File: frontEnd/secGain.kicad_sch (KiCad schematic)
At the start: 11 parts, among them U601 BGS12P2L6E6327XTSA1, U602 MSA-0286, U603 BGS12P2L6E6327XTSA1

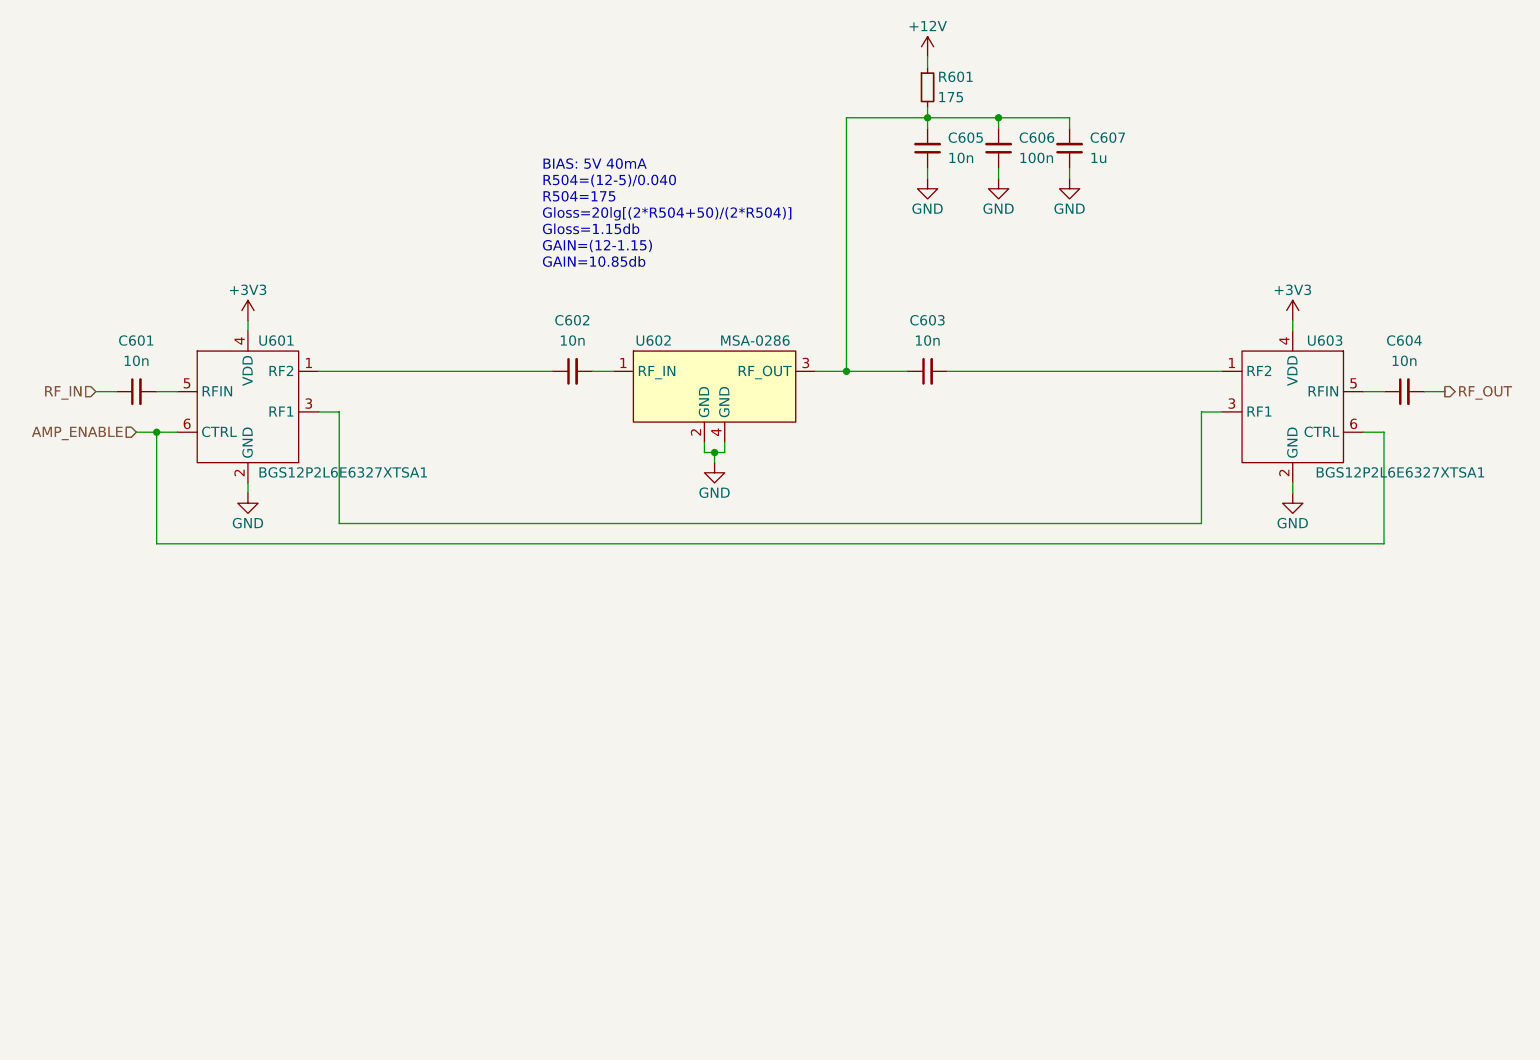
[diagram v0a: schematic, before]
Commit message: update schematics, add bypass for the attenuator
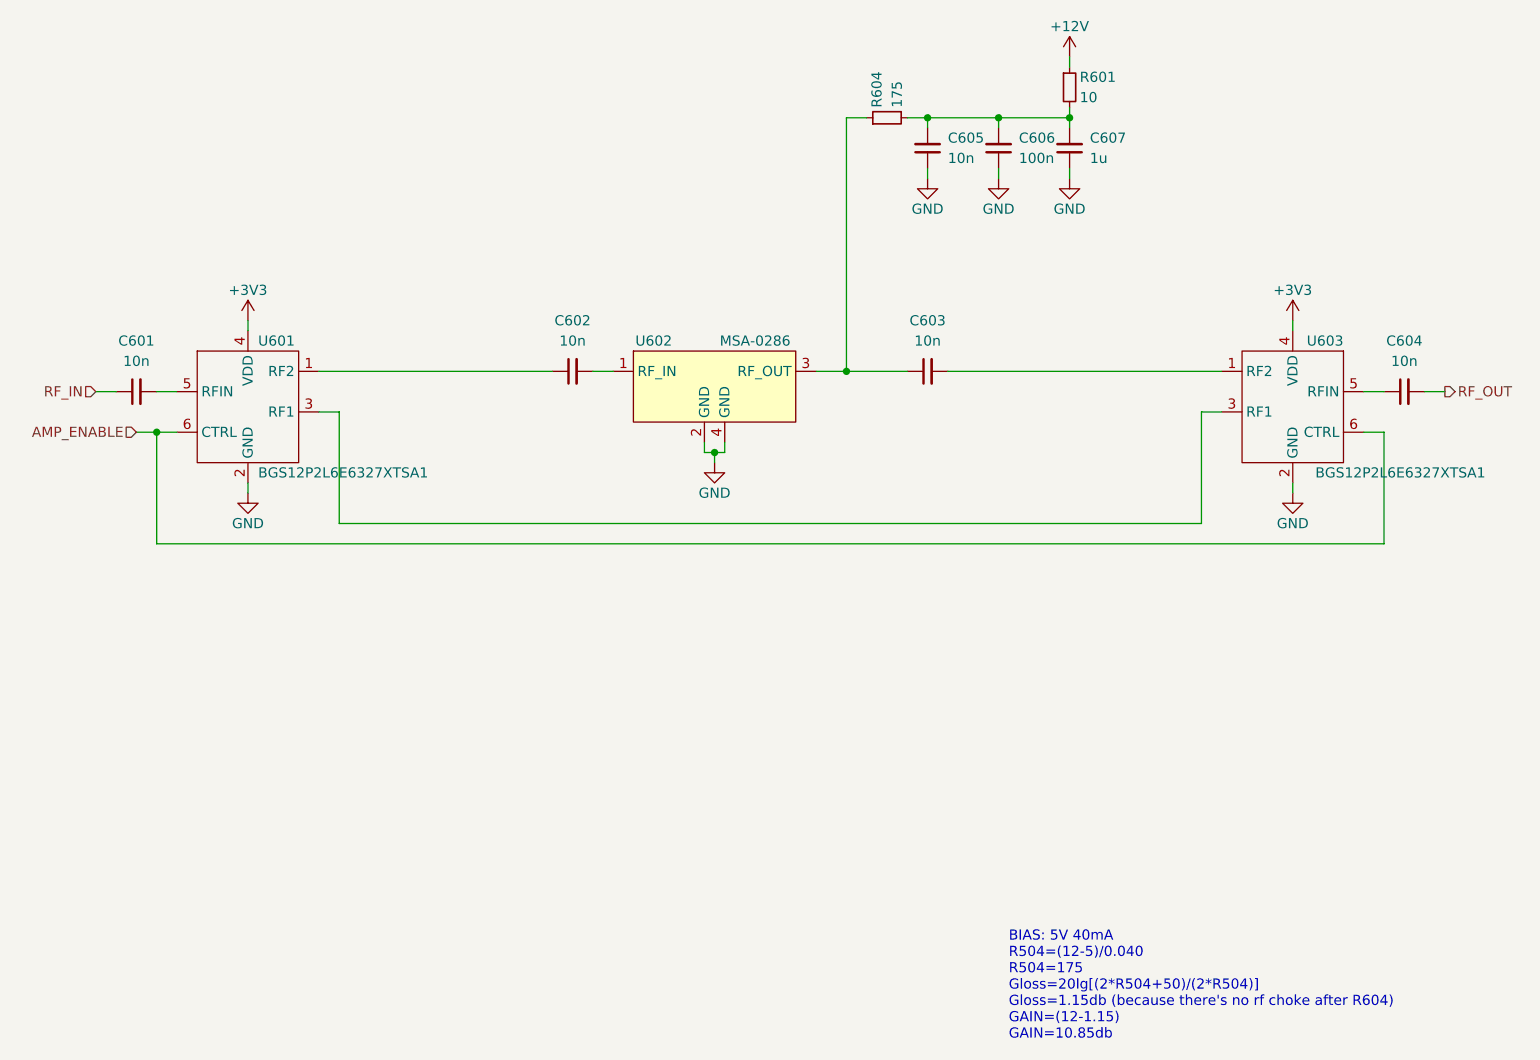
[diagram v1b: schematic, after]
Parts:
- added R601: 10, Resistor_SMD:R_0805_2012Metric, symbol Device:R_Small
- renumbered R601 to R604
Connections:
- net +12V: now also R601.1; no longer R604.1
- net at C605.2, C606.2, C607.2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: now also R601.2; no longer C603.1, U602.3 (RF_OUT)
- new net: C603.1, R604.1, U602.3 (RF_OUT)
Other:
- note added: "BIAS: 5V 40mA R504=(12-5)/0.040 R504=175 Gloss=20lg[(2*R504+50)/(2*R504)] Gloss=1.15db (because there's no rf choke after R604) GAIN=(12-1.15) GAIN=10.85db"
- note removed: "BIAS: 5V 40mA R504=(12-5)/0.040 R504=175 Gloss=20lg[(2*R504+50)/(2*R504)] Gloss=1.15db GAIN=(12-1.15) GAIN=10.85db"
- moved on the sheet: R604
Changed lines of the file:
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@@
   (junction (at 176.53 64.77) (diameter 0) (color 0 0 0 0)
   )
+  (junction (at 185.42 64.77) (diameter 0) (color 0 0 0 0)
+  )
   (wire (pts (xy 213.36 110.49) (xy 213.36 111.76))
     (stroke (width 0) (type default) (color 0 0 0 0))
@@
     (stroke (width 0) (type default) (color 0 0 0 0))
   )
-  (wire (pts (xy 157.48 64.77) (xy 167.64 64.77))
-    (stroke (width 0) (type default) (color 0 0 0 0))
-  )
   (wire (pts (xy 185.42 71.12) (xy 185.42 72.39))
     (stroke (width 0) (type default) (color 0 0 0 0))
@@
     (stroke (width 0) (type default) (color 0 0 0 0))
   )
+  (wire (pts (xy 165.1 64.77) (xy 167.64 64.77))
+    (stroke (width 0) (type default) (color 0 0 0 0))
+  )
   (wire (pts (xy 139.7 105.41) (xy 139.7 106.68))
     (stroke (width 0) (type default) (color 0 0 0 0))
   )
+  (wire (pts (xy 185.42 63.5) (xy 185.42 64.77))
+    (stroke (width 0) (type default) (color 0 0 0 0))
+  )
   (wire (pts (xy 68.58 104.14) (xy 71.12 104.14))
     (stroke (width 0) (type default) (color 0 0 0 0))
@@
     (stroke (width 0) (type default) (color 0 0 0 0))
   )
+  (wire (pts (xy 157.48 64.77) (xy 160.02 64.77))
+    (stroke (width 0) (type default) (color 0 0 0 0))
+  )
   (wire (pts (xy 222.25 99.06) (xy 224.79 99.06))
     (stroke (width 0) (type default) (color 0 0 0 0))
@@
     (stroke (width 0) (type default) (color 0 0 0 0))
   )
-  (wire (pts (xy 167.64 57.15) (xy 167.64 58.42))
-    (stroke (width 0) (type default) (color 0 0 0 0))
-  )
-  (wire (pts (xy 167.64 63.5) (xy 167.64 64.77))
-    (stroke (width 0) (type default) (color 0 0 0 0))
-  )
-  (text "BIAS: 5V 40mA\nR504=(12-5)/0.040\nR504=175\nGloss=20lg[(2*R504+50)/(2*R504)]\nGloss=1.15db\nGAIN=(12-1.15)\nGAIN=10.85db"
-    (at 119.38 83.82 0)
+  (wire (pts (xy 185.42 57.15) (xy 185.42 58.42))
+    (stroke (width 0) (type default) (color 0 0 0 0))
+  )
+  (text "BIAS: 5V 40mA\nR504=(12-5)/0.040\nR504=175\nGloss=20lg[(2*R504+50)/(2*R504)]\nGloss=1.15db (because there's no rf choke after R604)\nGAIN=(12-1.15)\nGAIN=10.85db"
+    (at 177.8 180.34 0)
     (effects (font (size 1.27 1.27)) (justify left bottom))
   )
@@
     (pin "2")
   )
-  (symbol (lib_id "power:+12V") (at 167.64 57.15 0) (unit 1)
-    (in_bom yes) (on_board yes)
-    (property "Reference" "#PWR?" (id 0) (at 167.64 60.96 0)
-      (effects (font (size 1.27 1.27)) hide)
-    )
-    (property "Value" "+12V" (id 1) (at 167.64 53.34 0))
-    (property "Footprint" "" (id 2) (at 167.64 57.15 0)
-      (effects (font (size 1.27 1.27)) hide)
-    )
-    (property "Datasheet" "" (id 3) (at 167.64 57.15 0)
+  (symbol (lib_id "power:+12V") (at 185.42 57.15 0) (unit 1)
+    (in_bom yes) (on_board yes)
+    (property "Reference" "#PWR?" (id 0) (at 185.42 60.96 0)
+      (effects (font (size 1.27 1.27)) hide)
+    )
+    (property "Value" "+12V" (id 1) (at 185.42 53.34 0))
+    (property "Footprint" "" (id 2) (at 185.42 57.15 0)
+      (effects (font (size 1.27 1.27)) hide)
+    )
+    (property "Datasheet" "" (id 3) (at 185.42 57.15 0)
       (effects (font (size 1.27 1.27)) hide)
     )
@@
     (pin "6")
   )
-  (symbol (lib_id "Device:R_Small") (at 167.64 60.96 0) (unit 1)
-    (in_bom yes) (on_board yes)
-    (property "Reference" "R601" (id 0) (at 168.91 59.69 0)
-      (effects (font (size 1.27 1.27)) (justify left))
-    )
-    (property "Value" "175" (id 1) (at 168.91 62.23 0)
-      (effects (font (size 1.27 1.27)) (justify left))
-    )
-    (property "Footprint" "Resistor_SMD:R_0805_2012Metric" (id 2) (at 167.64 60.96 0)
-      (effects (font (size 1.27 1.27)) hide)
-    )
-    (property "Datasheet" "~" (id 3) (at 167.64 60.96 0)
+  (symbol (lib_id "Device:R_Small") (at 162.56 64.77 90) (unit 1)
+    (in_bom yes) (on_board yes)
+    (property "Reference" "R604" (id 0) (at 161.29 63.5 0)
+      (effects (font (size 1.27 1.27)) (justify left))
+    )
+    (property "Value" "175" (id 1) (at 163.83 63.5 0)
+      (effects (font (size 1.27 1.27)) (justify left))
+    )
+    (property "Footprint" "Resistor_SMD:R_0805_2012Metric" (id 2) (at 162.56 64.77 0)
+      (effects (font (size 1.27 1.27)) hide)
+    )
+    (property "Datasheet" "~" (id 3) (at 162.56 64.77 0)
       (effects (font (size 1.27 1.27)) hide)
     )
@@
     (pin "1")
   )
+  (symbol (lib_id "Device:R_Small") (at 185.42 60.96 0) (unit 1)
+    (in_bom yes) (on_board yes)
+    (property "Reference" "R601" (id 0) (at 186.69 59.69 0)
+      (effects (font (size 1.27 1.27)) (justify left))
+    )
+    (property "Value" "10" (id 1) (at 186.69 62.23 0)
+      (effects (font (size 1.27 1.27)) (justify left))
+    )
+    (property "Footprint" "Resistor_SMD:R_0805_2012Metric" (id 2) (at 185.42 60.96 0)
+      (effects (font (size 1.27 1.27)) hide)
+    )
+    (property "Datasheet" "~" (id 3) (at 185.42 60.96 0)
+      (effects (font (size 1.27 1.27)) hide)
+    )
+    (pin "1")
+    (pin "2")
+  )
 )
